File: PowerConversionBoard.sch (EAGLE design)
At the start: 37 parts, among them U1 LM2678, U2 LM2678

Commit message: Added LED and test points
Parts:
- added LED4: (no value), led:LEDCHIP-LED0603
- added R1: 470, SparkFun-Resistors:470OHM-0603-1/10W-1%
- added U$10, U$11, U$12, U$6, U$7, U$8, U$9: TP, TP:TP
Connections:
- new net GND1: C15.-, C16.-, C17.-, C18.-, C7.2
- new net N$20: U1.VIN
- new net N$6: LED4.A, R1.1
- net +12V: now also U$7.P$1
- net +3.3V: now also U$6.P$1
- net +5V: now also U$11.P$1
- net +5V_3.3V: now also R1.2, U$8.P$1
- net GND: now also LED4.C, U$10.P$1, U$9.P$1; no longer C15.-, C16.-, C17.-, C18.-, C7.2
- net N$4: now also U$12.P$1; no longer U1.VIN
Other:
- moved on the sheet: C15, C16, C17, C18, C7

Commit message: board work
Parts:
- removed U$9: TP, TP:TP
- added J3, J4: (no value), SparkFun-Connectors:BANANA_CONN
- added U$14: TP, TP:TP
- U$7: value TP -> CONVERSION_TSW_12X2; device TP:TP -> Conversion_Connector:CONVERSION_TSW_12X2
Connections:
- removed net GND1: C15.-, C16.-, C17.-, C18.-, C7.2
- removed net N$4: C15.+, C16.+, C17.+, C18.+, C7.1, U$12.P$1
- net +12V: now also U$12.P$1, U$14.P$1; no longer U$7.P$1
- net +5V: now also U$10.P$1; no longer U$11.P$1
- net +5V_3.3V: now also J4.1
- net GND: now also C15.-, C16.-, C17.-, C18.-, C7.2, J3.1, U$11.P$1; no longer U$10.P$1, U$9.P$1
- net N$20: now also C15.+, C16.+, C17.+, C18.+, C7.1
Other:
- note added: "Pins"
- note added: "Test Points"
- moved on the sheet: J1, J2, J5, J6, U$10, U$11, U$12, U$6, U$8

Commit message: updates
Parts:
- removed LED1, LED2, LED3, LED4: (no value), led:LEDCHIP-LED0603
- added D1, D2, D3, D4: (no value), SparkFun-LED:LED0603
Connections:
- new net N$4: D2.A, R5.1
- new net N$8: D1.A, R2.1
- net GND: now also D1.C, D2.C, D3.C, D4.C; no longer LED1.C, LED2.C, LED3.C, LED4.C
- net N$5: now also D3.A; no longer LED3.A
- net N$6: now also D4.A; no longer LED4.A

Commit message: updated board
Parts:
- removed U$7: CONVERSION_TSW_12X2, Conversion_Connector:CONVERSION_TSW_12X2
- added U$9: CONVERSION_TSW_12X2, Dist_to_Conversion_Connector:CONVERSION_TSW_12X2

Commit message: Did some stuff
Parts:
- removed U$12, U$14: TP, TP:TP
- added U$7: HCM1305, HCM1305:HCM1305
- U$5: value HCM1305 -> TP; device HCM1305:HCM1305 -> TP:TP
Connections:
- net +12V: now also U$5.P$1; no longer U$12.P$1, U$14.P$1
- net +5V: now also U$11.P$1, U$2.2; no longer U$10.P$1, U$5.2
- net +5V_3.3V: now also U$7.2; no longer U$2.2
- net GND: now also U$10.P$1; no longer U$11.P$1
- net N$1: now also U$2.1; no longer U$5.1
- net N$7: now also U$7.1; no longer U$2.1
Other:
- moved on the sheet: U$10, U$11, U$2

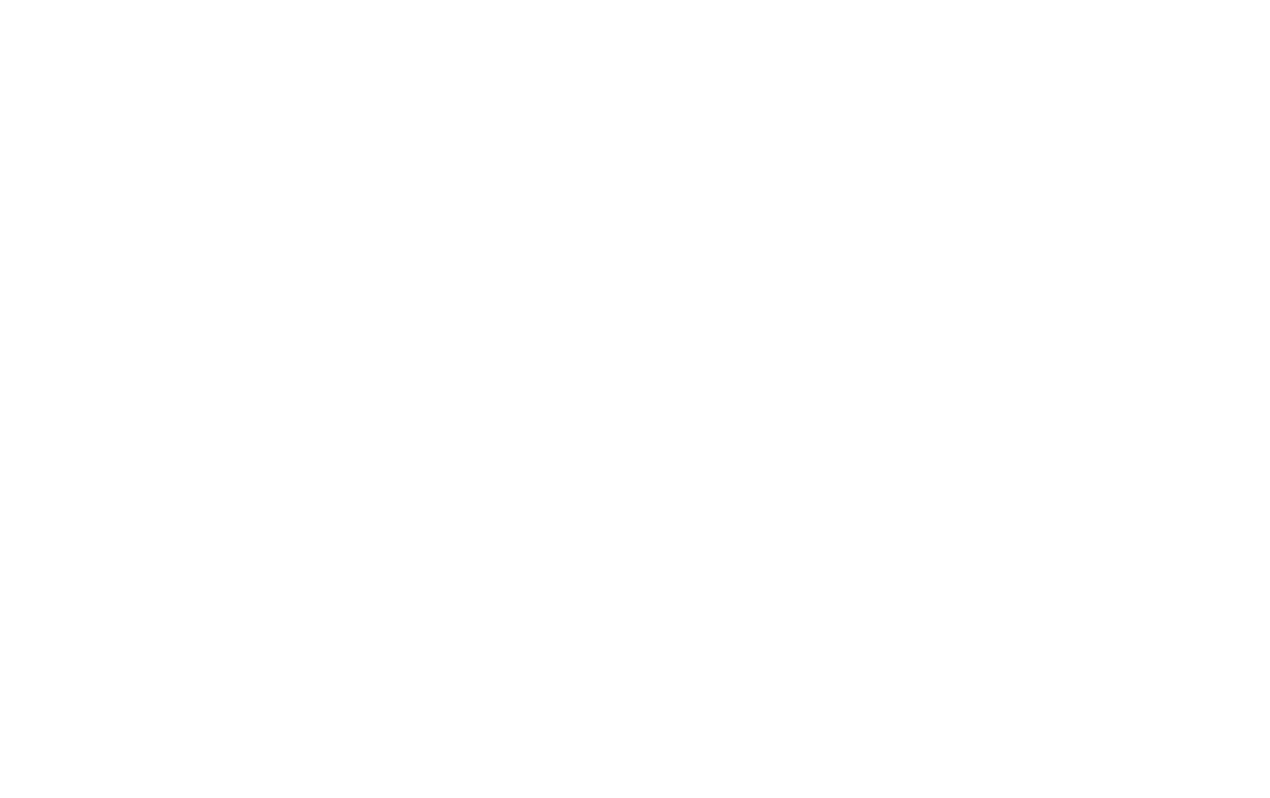
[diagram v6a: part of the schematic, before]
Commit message: added connector for backplane
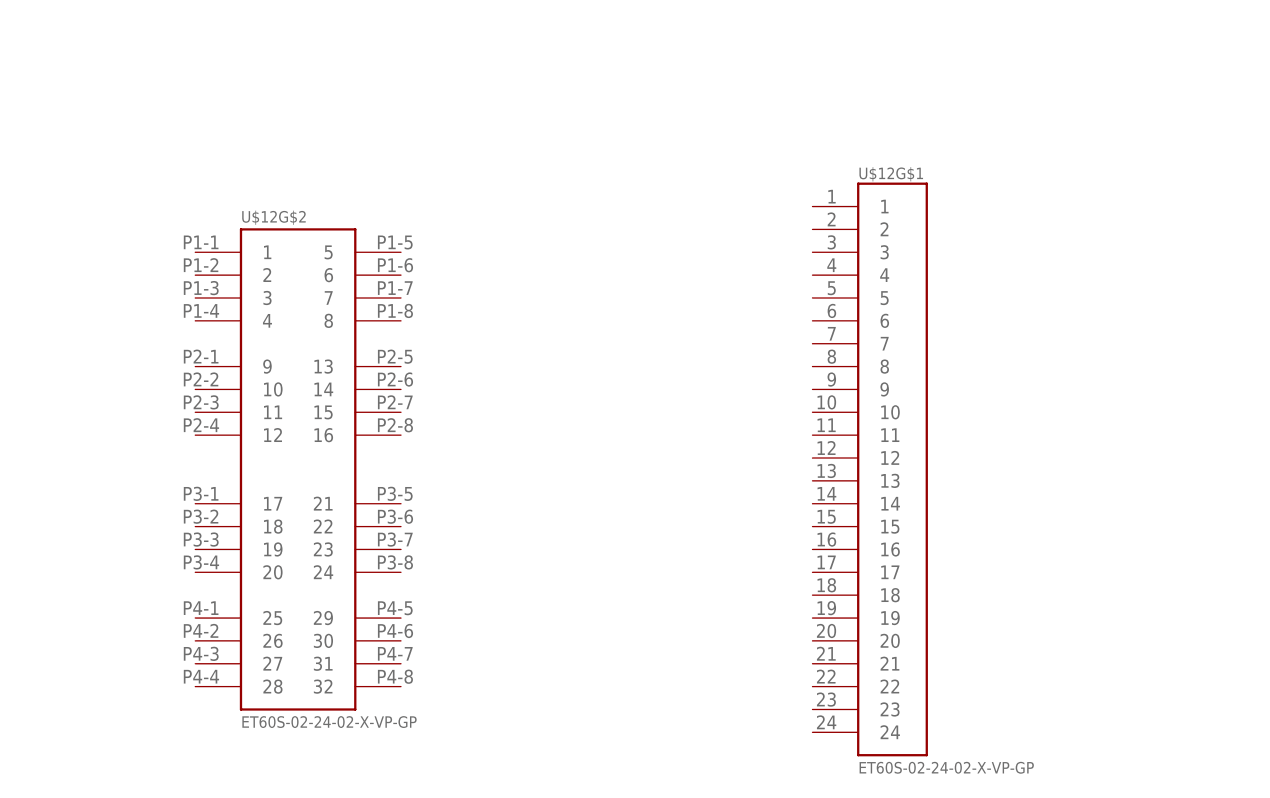
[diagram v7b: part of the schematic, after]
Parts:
- added U$12: ET60S-02-24-02-X-VP-GP, ET60S-02-24-02-X-VP-GP:ET60S-02-24-02-X-VP-GP

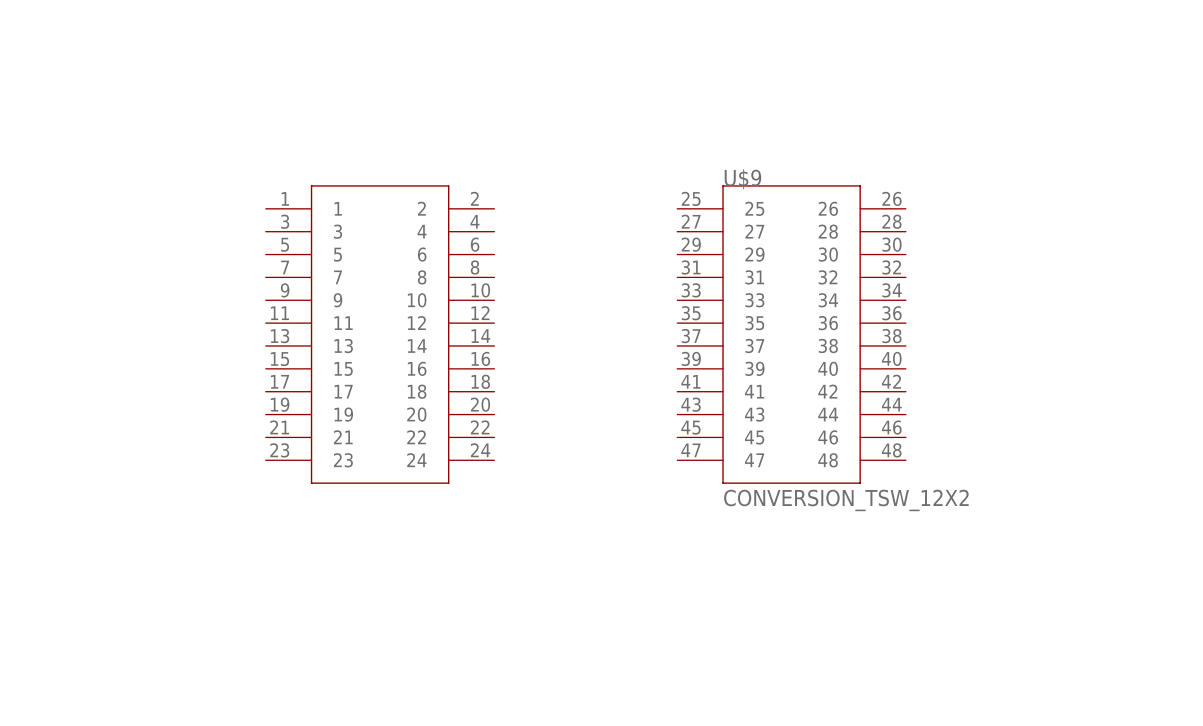
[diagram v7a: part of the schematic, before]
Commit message: power plane
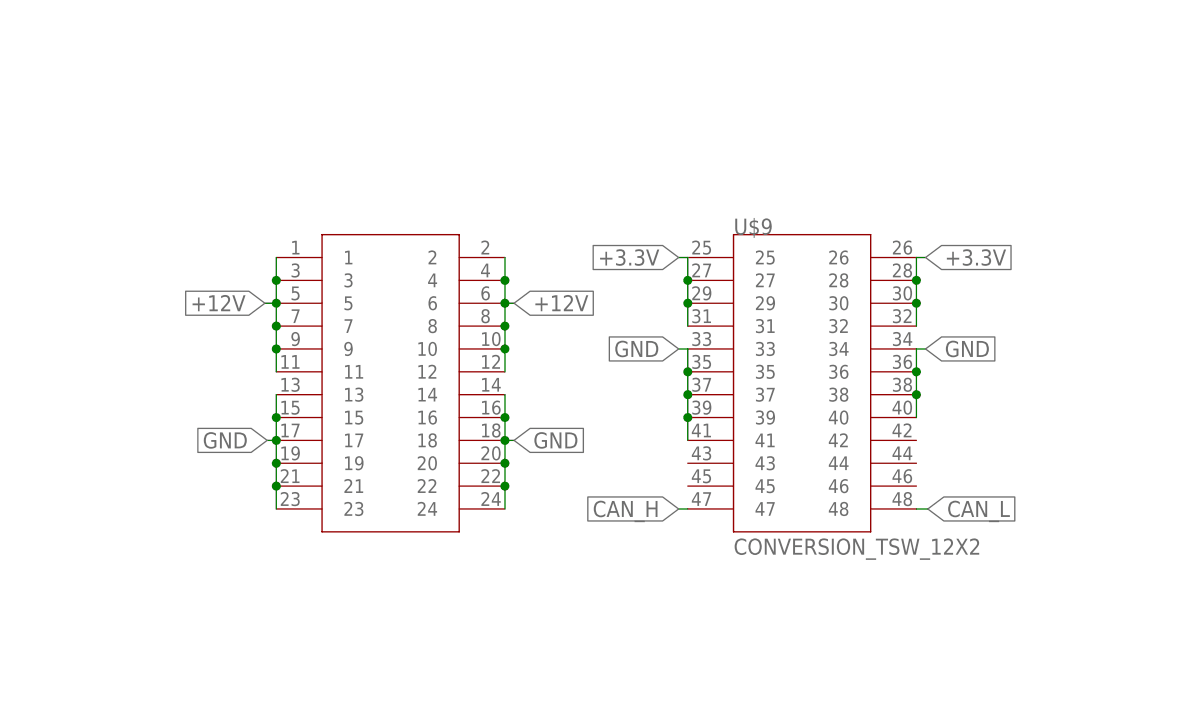
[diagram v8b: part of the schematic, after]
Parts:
- U$9: device Dist_to_Conversion_Connector:CONVERSION_TSW_12X2 -> Conversion_Connector:CONVERSION_TSW_12X2
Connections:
- new net CAN_H: U$9.47
- new net CAN_L: U$9.48
- net +12V: now also U$9.1, U$9.10, U$9.11, U$9.12, U$9.2, U$9.3, U$9.4, U$9.5, U$9.6, U$9.7, U$9.8, U$9.9
- net +3.3V: now also U$9.25, U$9.26, U$9.27, U$9.28, U$9.29, U$9.30, U$9.31, U$9.32
- net GND: now also U$9.13, U$9.14, U$9.15, U$9.16, U$9.17, U$9.18, U$9.19, U$9.20, U$9.21, U$9.22, U$9.23, U$9.24, U$9.33, U$9.34, U$9.35, U$9.36, U$9.37, U$9.38, U$9.39, U$9.40, U$9.41
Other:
- moved on the sheet: U$9
